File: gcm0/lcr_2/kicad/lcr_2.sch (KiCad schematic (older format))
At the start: 119 parts, among them J1 5V, J2 -5V, J3 Conn_01x01_Male, J4 Conn_01x03_Male, J5 Conn_01x01_Male, J6 Conn_01x01_Male, J8 SWD, Q1 BC547, Q2 BC547, Q3 BC547, SW1 1, SW2 2, U1 RC4580, U10 RC4580, U11 74HC595, U12 STM32F030F4P6, U2 74HC4053PW,112, U3 74HC4052PW,118, U4 RC4580, U5 LM2596S-5, U6 LM7805_TO220, U7 RC4580, U8 LM1117-3.3, U9 74HC4053PW,112, Y1 8M

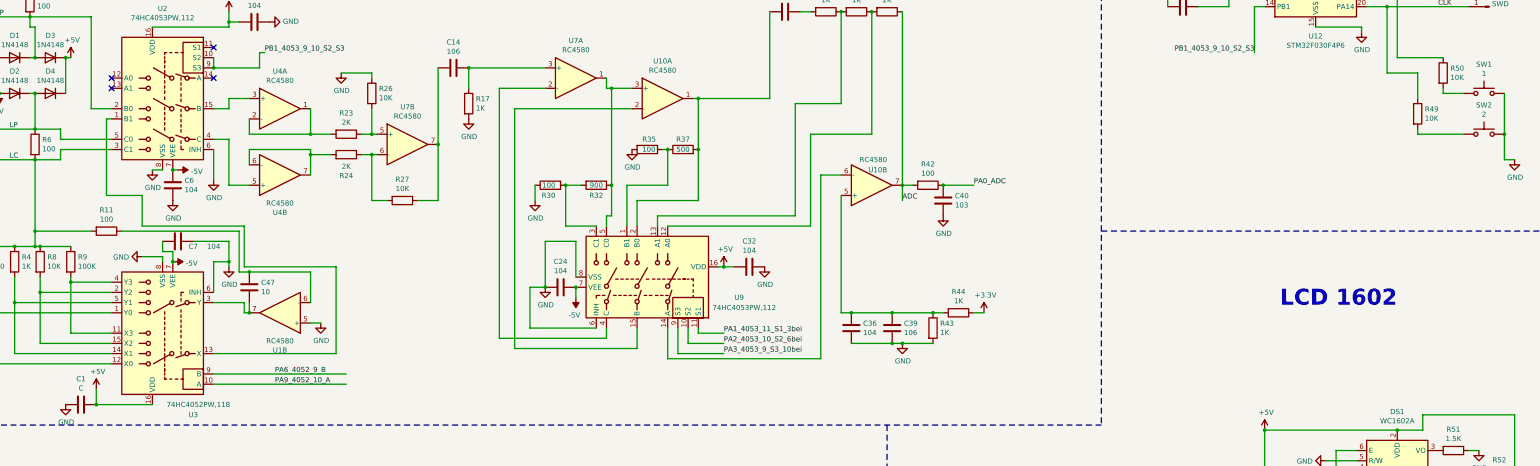
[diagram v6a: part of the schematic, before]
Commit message: 自动档位改错
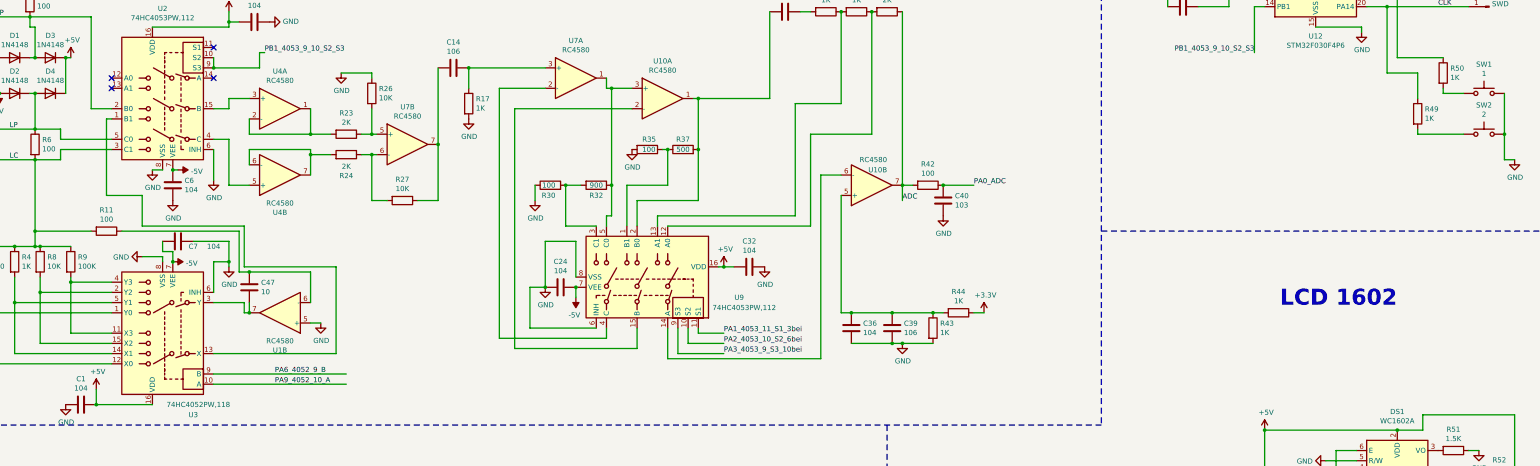
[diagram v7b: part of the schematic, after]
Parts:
- C1: value C -> 104
- R49, R50: value 10K -> 1K
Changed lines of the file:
@@
 P 15100 3850
 F 0 "R50" H 15170 3896 50  0000 L CNN
-F 1 "10K" H 15170 3805 50  0000 L CNN
+F 1 "1K" H 15170 3805 50  0000 L CNN
 F 2 "Resistor_THT:R_Axial_DIN0204_L3.6mm_D1.6mm_P1.90mm_Vertical" V 15030 3850 50  0001 C CNN
 F 3 "~" H 15100 3850 50  0001 C CNN
@@
 P 14850 4250
 F 0 "R49" H 14920 4296 50  0000 L CNN
-F 1 "10K" H 14920 4205 50  0000 L CNN
+F 1 "1K" H 14920 4205 50  0000 L CNN
 F 2 "Resistor_THT:R_Axial_DIN0204_L3.6mm_D1.6mm_P1.90mm_Vertical" V 14780 4250 50  0001 C CNN
 F 3 "~" H 14850 4250 50  0001 C CNN
@@
 P 1750 7100
 F 0 "C1" V 1498 7100 50  0000 C CNN
-F 1 "C" V 1589 7100 50  0000 C CNN
+F 1 "104" V 1589 7100 50  0000 C CNN
 F 2 "Capacitor_SMD:C_0603_1608Metric_Pad1.08x0.95mm_HandSolder" H 1788 6950 50  0001 C CNN
 F 3 "~" H 1750 7100 50  0001 C CNN
